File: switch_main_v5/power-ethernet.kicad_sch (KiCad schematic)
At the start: 26 parts, among them U501 TPS62290TDRVRQ1, U502 TPS62290TDRVRQ1

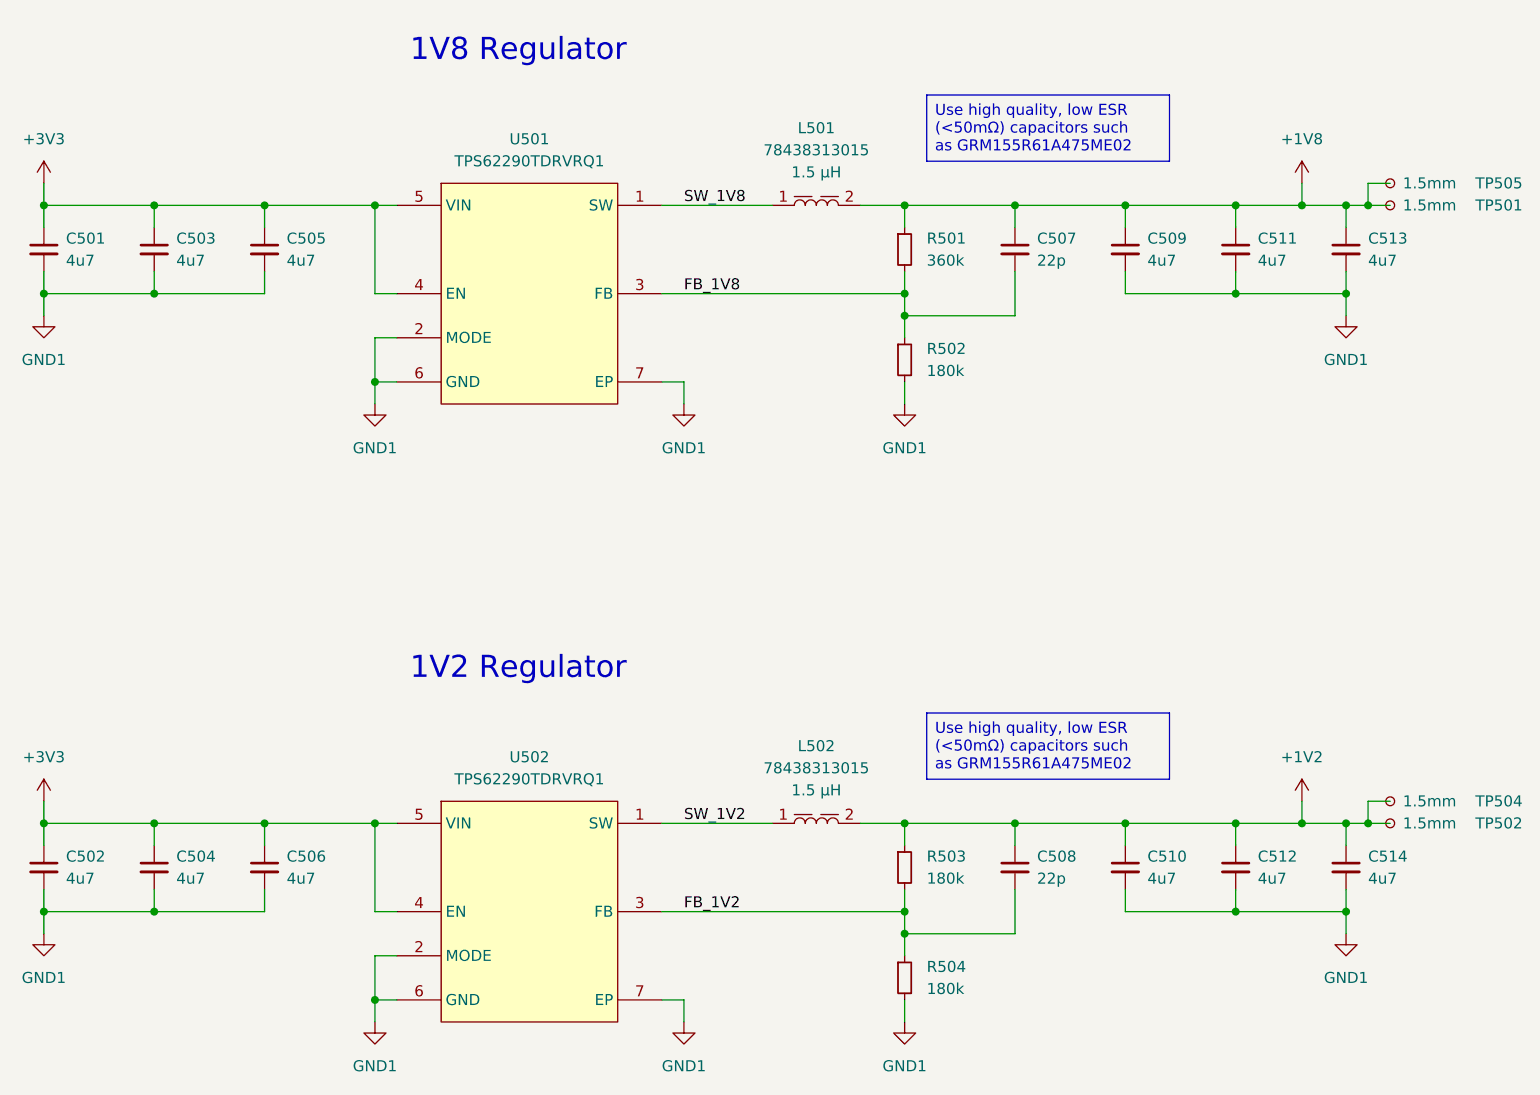
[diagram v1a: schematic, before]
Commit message: Started updating regulators for v5
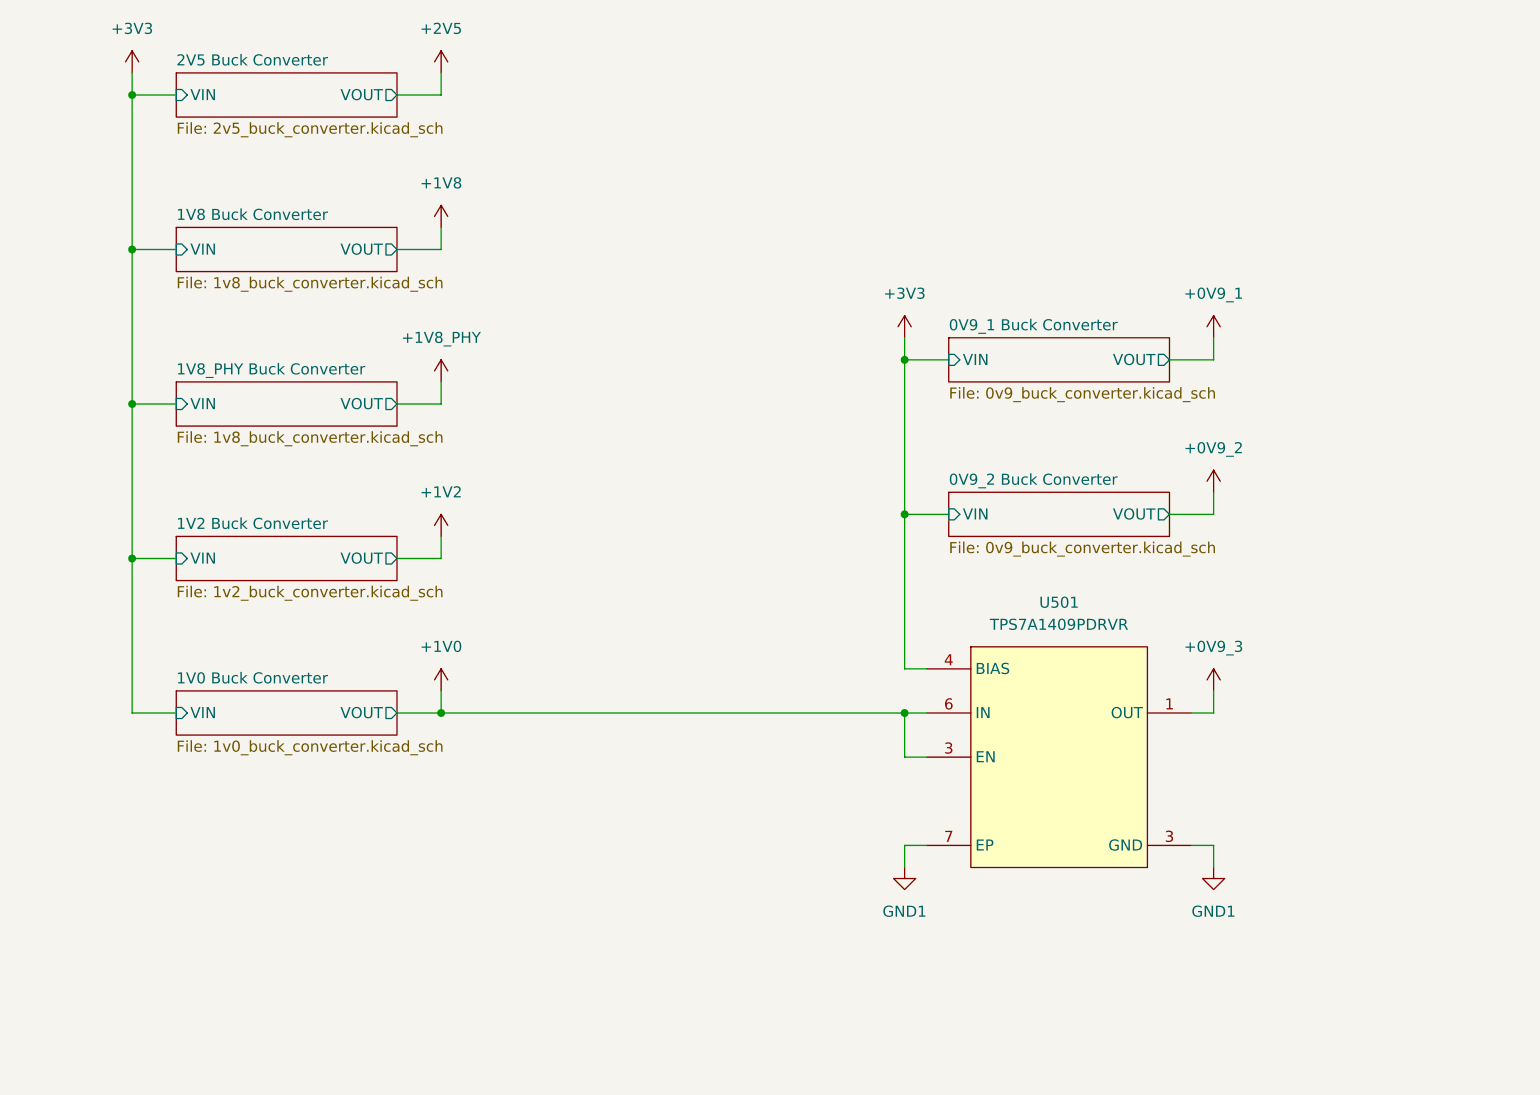
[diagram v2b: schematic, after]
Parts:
- removed C501, C502, C503, C504, C505, C506, C509, C510, C511, C512, C513, C514: 4u7, Capacitor_SMD:C_0402_1005Metric, symbol Device:C_Small
- removed C507, C508: 22p, Capacitor_SMD:C_0402_1005Metric, symbol Device:C_Small
- removed L501, L502: 78438313015, project_footprints:L_Wurth_WE-MAIA-1610, symbol PWR-IND:1610_78438313015
- removed R501: 360k, Resistor_SMD:R_0402_1005Metric, symbol Device:R_Small
- removed R502, R503, R504: 180k, Resistor_SMD:R_0402_1005Metric, symbol Device:R_Small
- removed TP501, TP502, TP504, TP505: 1.5mm, TestPoint:TestPoint_Pad_D1.5mm, symbol Connector:TestPoint_Small
- removed U501, U502: TPS62290TDRVRQ1, project_footprints:SON65P200X200X80-7N, symbol PWR-SMPS:TPS62290TDRVRQ1
- added U501: TPS7A1409PDRVR, project_footprints:SON65P200X200X80-7N, symbol PWR-LDO:TPS7A1409PDRVR
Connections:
- net +3V3: now also U501.4 (BIAS)
- net GND1: now also U501.3 (GND), U501.7 (EP)
- new net +0V9_3: U501.1 (OUT)
- new net +1V0: U501.3 (GND), U501.6 (IN)
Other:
- added sheet 0V9_1 Buck Converter (0v9_buck_converter.kicad_sch)
- added sheet 0V9_2 Buck Converter (0v9_buck_converter.kicad_sch)
- added sheet 1V0 Buck Converter (1v0_buck_converter.kicad_sch)
- added sheet 1V2 Buck Converter (1v2_buck_converter.kicad_sch)
- added sheet 1V8 Buck Converter (1v8_buck_converter.kicad_sch)
- added sheet 1V8_PHY Buck Converter (1v8_buck_converter.kicad_sch)
- added sheet 2V5 Buck Converter (2v5_buck_converter.kicad_sch)
- note removed: "1V2 Regulator"
- note removed: "1V8 Regulator"

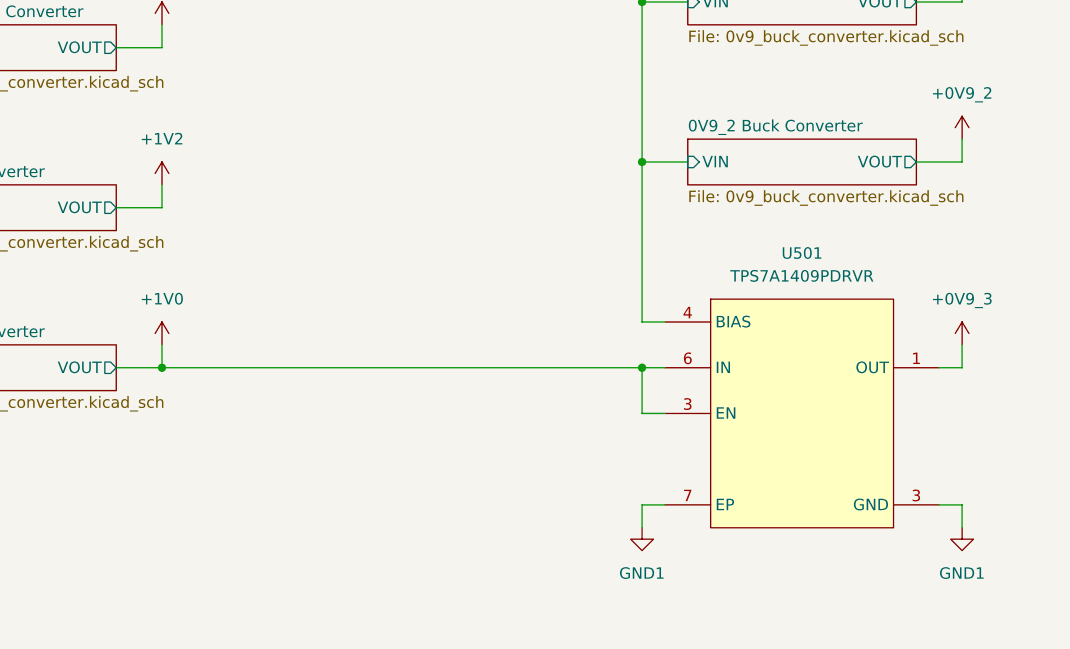
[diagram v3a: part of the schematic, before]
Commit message: Changed main 3V3 regulator to 3A, added switch 2 crystal & other changes
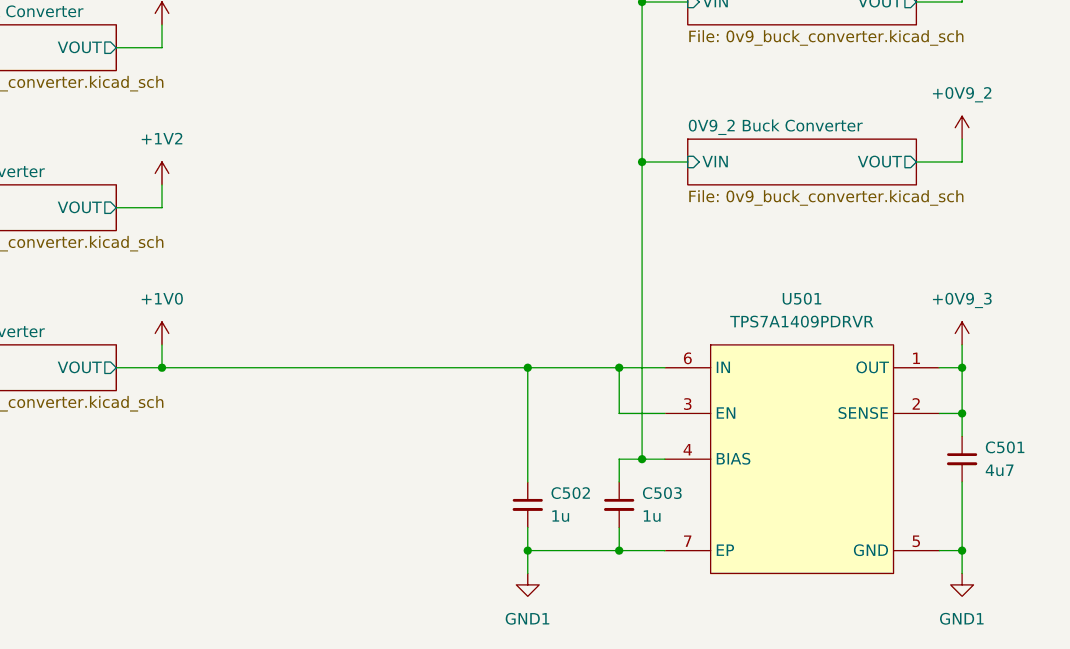
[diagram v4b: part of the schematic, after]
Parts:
- added C501: 4u7, Capacitor_SMD:C_0402_1005Metric, symbol Device:C_Small
- added C502, C503: 1u, Capacitor_SMD:C_0402_1005Metric, symbol Device:C_Small
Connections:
- net +0V9_3: now also U501.2 (SENSE), C501.1
- net +1V0: now also C502.1
- net +3V3: now also C503.1
- net GND1: now also U501.5 (GND), C501.2, C502.2, C503.2; no longer U501.3 (GND)

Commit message: Fixed test points
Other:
- removed sheet 2V5 Buck Converter
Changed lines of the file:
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@@
 		(comment 4 "1V8 and 1V2 SMPS for ethernet switch and PHYs.")
+	)
+	(text_box "TPS7A2025PDQNR"
+		(exclude_from_sim no)
+		(at 93.98 35.56 0)
+		(size 25.4 10.16)
+		(margins 0.9525 0.9525 0.9525 0.9525)
+		(stroke
+			(width 0)
+			(type solid)
+			(color 255 0 0 1)
+		)
+		(fill
+			(type none)
+		)
+		(effects
+			(font
+				(size 1.27 1.27)
+				(color 255 0 0 1)
+			)
+		)
 	)
 	(junction
@@
 				)
 			)
-		)
-	)
-	(sheet
-		(at 93.98 38.1)
-		(size 25.4 5.08)
-		(exclude_from_sim no)
-		(in_bom yes)
-		(on_board yes)
-		(dnp no)
-		(fields_autoplaced yes)
-		(stroke
-			(width 0.1524)
-			(type solid)
-		)
-		(fill
-			(color 0 0 0 0.0000)
-		)
-		(property "Sheetname" "2V5 Buck Converter"
-			(at 93.98 37.3884 0)
-			(effects
-				(font
-					(size 1.27 1.27)
-				)
-				(justify left bottom)
-			)
-		)
-		(property "Sheetfile" "2v5_buck_converter.kicad_sch"
-			(at 93.98 43.7646 0)
-			(effects
-				(font
-					(size 1.27 1.27)
-				)
-				(justify left top)
-			)
-		)
-		(pin "VIN" input
-			(at 93.98 40.64 180)
-			(effects
-				(font
-					(size 1.27 1.27)
-				)
-				(justify left)
-			)
-		)
-		(pin "VOUT" output
-			(at 119.38 40.64 0)
-			(effects
-				(font
-					(size 1.27 1.27)
-				)
-				(justify right)
-			)
-		)
-		(instances
-			(project "switch_main_v5"
-				(path "/a5e57332-4284-4d3c-ab3c-13bc0ddb29b6/b1ff42f5-7cae-489e-9f8e-588cc93f3151/d017dddd-15df-4565-b589-89c8c78bc85c"
-					(page "37")
-				)
-			)

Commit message: Moved 0V9 regulators
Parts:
- added C504, C505: 1u, Capacitor_SMD:C_0402_1005Metric, symbol Device:C_Small
- added U502: TPS7A2025PDQNR, project_footprints:DQN0004A-MFG, symbol PWR-LDO:TPS7A2025PDQNR
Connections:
- net +2V5: now also C504.1, U502.1 (OUT)
- net +3V3: now also C505.1, U502.3 (EN), U502.4 (IN)
- net GND1: now also C504.2, C505.2, U502.2 (GND), U502.5 (EP)

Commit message: Placed most remaining passives and test points
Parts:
- added TP501: 1.5mm, TestPoint:TestPoint_Pad_D1.5mm, symbol Connector:TestPoint_Small
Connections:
- net +0V9_3: now also TP501.1

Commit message: Fixed DRC issues and filleted outer layer traces
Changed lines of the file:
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@@
 		(comment 4 "1V8 and 1V2 SMPS for ethernet switch and PHYs.")
-	)
-	(text_box "Check LDO schematics"
-		(exclude_from_sim no)
-		(at 142.24 132.08 0)
-		(size 12.7 5.08)
-		(margins 0.9525 0.9525 0.9525 0.9525)
-		(stroke
-			(width 0)
-			(type solid)
-			(color 255 0 0 1)
-		)
-		(fill
-			(type none)
-		)
-		(effects
-			(font
-				(size 1.27 1.27)
-				(color 255 0 0 1)
-			)
-			(justify left top)
-		)
 	)
 	(junction
